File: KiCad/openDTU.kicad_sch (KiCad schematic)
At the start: 45 parts, among them J1 USB_C_Receptacle_USB2.0, J2 Conn_Coaxial, J3 Micro_SD_Card, Q1 BC817, Q2 BC817, SW1 SW_Push, SW2 SW_Push, U1 CH340C, U3 ESP32-WROOM-32, U4 nRF24L01P, U5 NCP1117-3.3_SOT223, Y1 Crystal

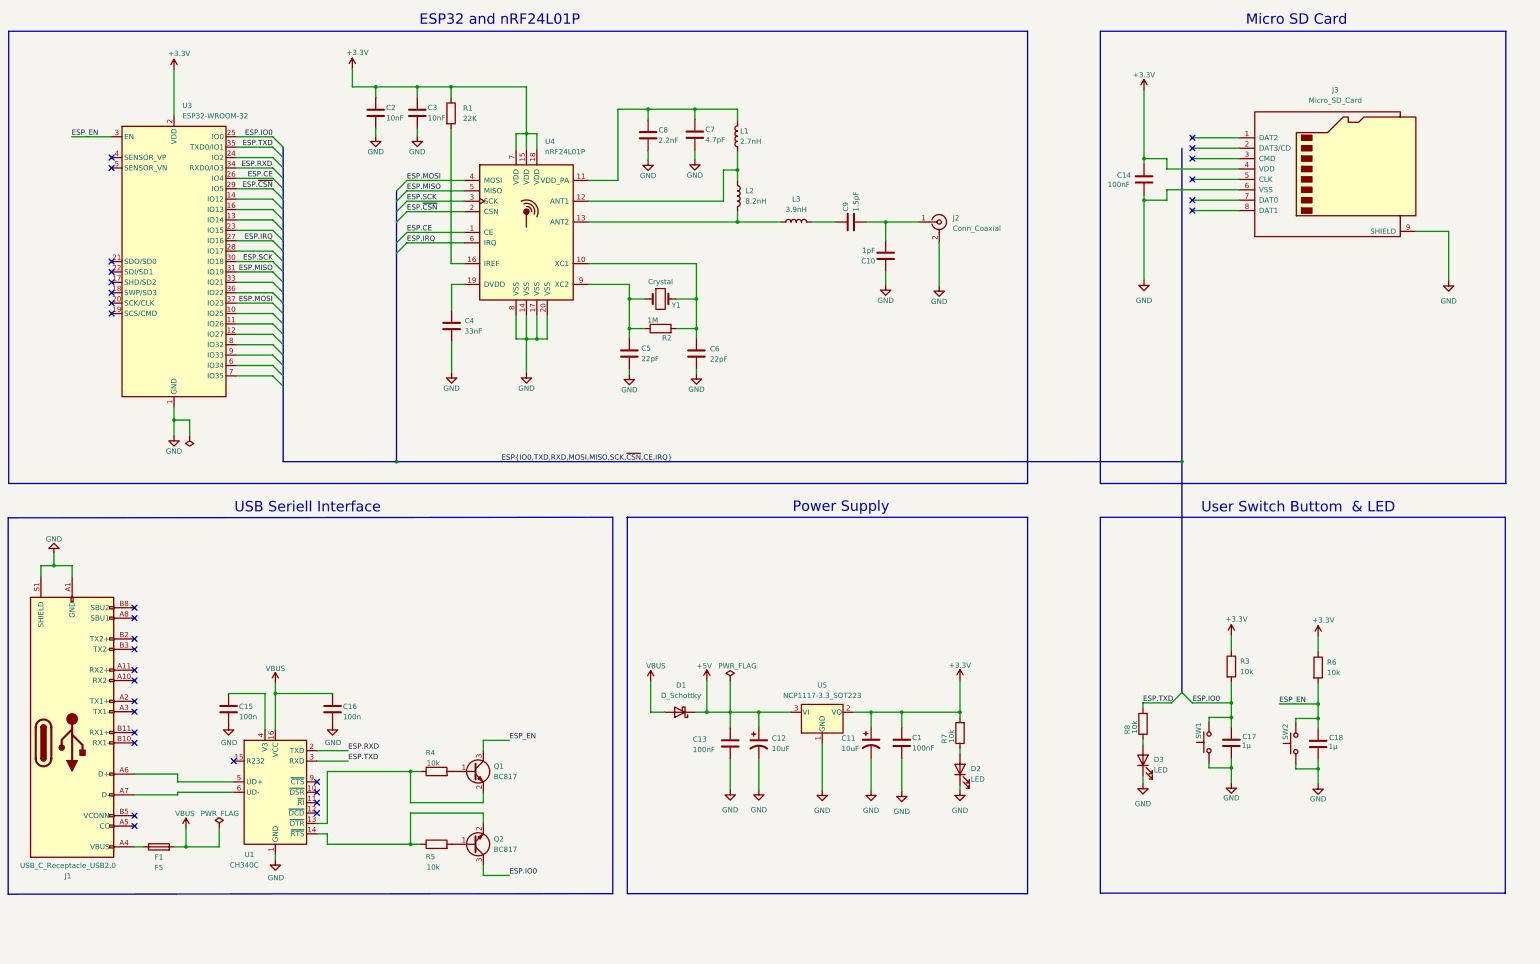
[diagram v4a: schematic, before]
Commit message: reduce the board size and beautify the placement
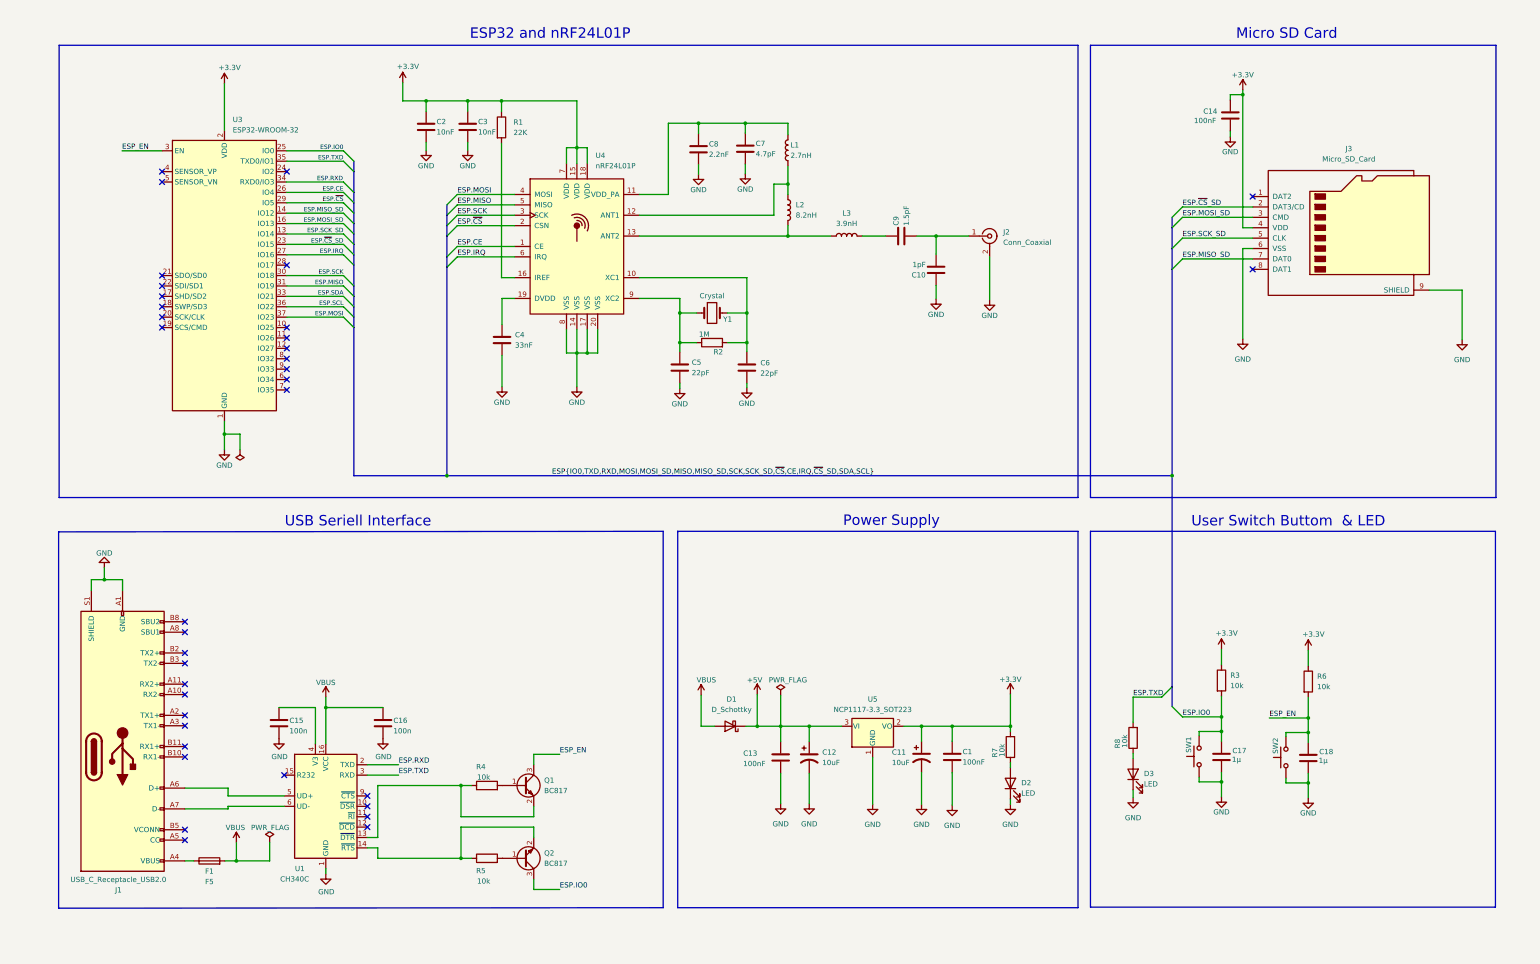
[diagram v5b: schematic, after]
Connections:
- net ESP.SCK_SD: now reaches U3.13 (IO14)
- net ESP.SCK_SD: now also J3.5 (CLK)
- net ESP.MISO_SD: now reaches U3.14 (IO12)
- net ESP.MISO_SD: now also J3.7 (DAT0)
- net ESP.MOSI_SD: now reaches U3.16 (IO13)
- net ESP.MOSI_SD: now also J3.3 (CMD)
- net ESP.~{CS}_SD: now reaches U3.23 (IO15)
- net ESP.~{CS}_SD: now also J3.2 (DAT3/CD)
- net ESP.SDA: now reaches U3.33 (IO21)
- net ESP.SCL: now reaches U3.36 (IO22)
- net ESP.~{CSN} renamed ESP.~{CS}
- no-connect marks 31 -> 36
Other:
- moved on the sheet: C1, C10, C11, C12, C13, C14, C15, C16, C17, C18, C2, C3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

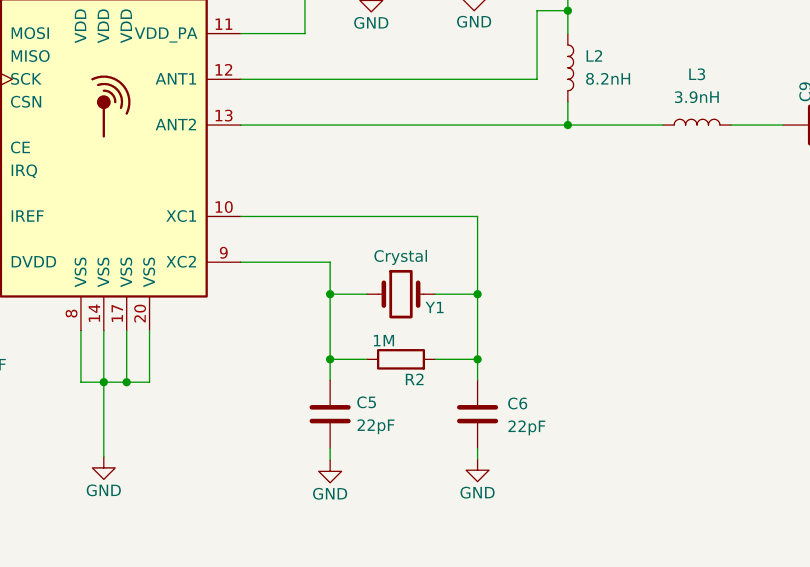
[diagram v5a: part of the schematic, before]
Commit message: routing first parts
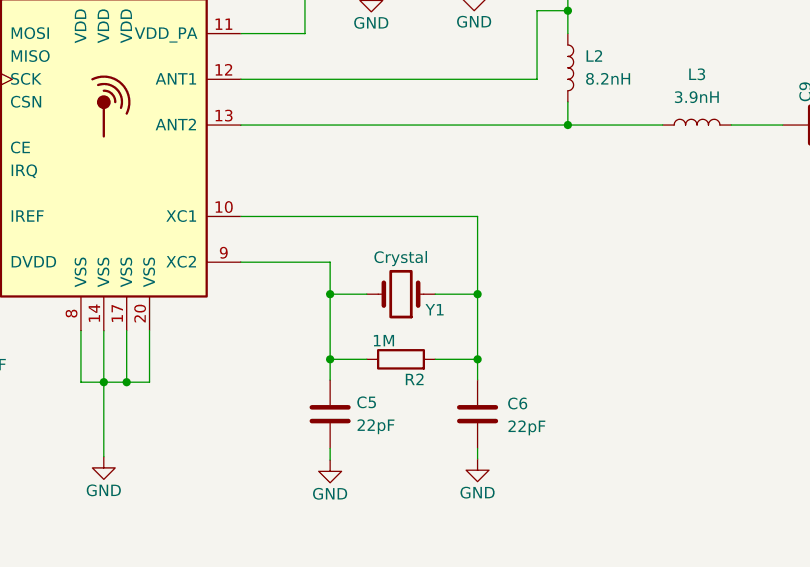
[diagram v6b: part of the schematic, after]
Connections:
- net at C5.1, R2.1, U4.9 (XC2): now also Y1.2; no longer Y1.1
- net at C6.1, R2.2, U4.10 (XC1): now also Y1.1; no longer Y1.2
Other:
- moved on the sheet: Y1
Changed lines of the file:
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@@
     (pin "1")
   )
-  (symbol (lib_id "Device:Crystal") (at 193.421 91.694 0) (unit 1)
+  (symbol (lib_id "Device:Crystal") (at 193.421 91.694 180) (unit 1)
     (in_bom yes) (on_board yes)
-    (property "Reference" "Y1" (id 0) (at 197.231 93.218 0))
-    (property "Value" "Crystal" (id 1) (at 193.421 87.503 0))
+    (property "Reference" "Y1" (id 0) (at 197.231 93.472 0))
+    (property "Value" "Crystal" (id 1) (at 193.421 87.63 0))
     (property "Footprint" "Crystal:Crystal_SMD_3225-4Pin_3.2x2.5mm" (id 2) (at 193.421 91.694 0)
       (effects (font (size 1.27 1.27)) hide)

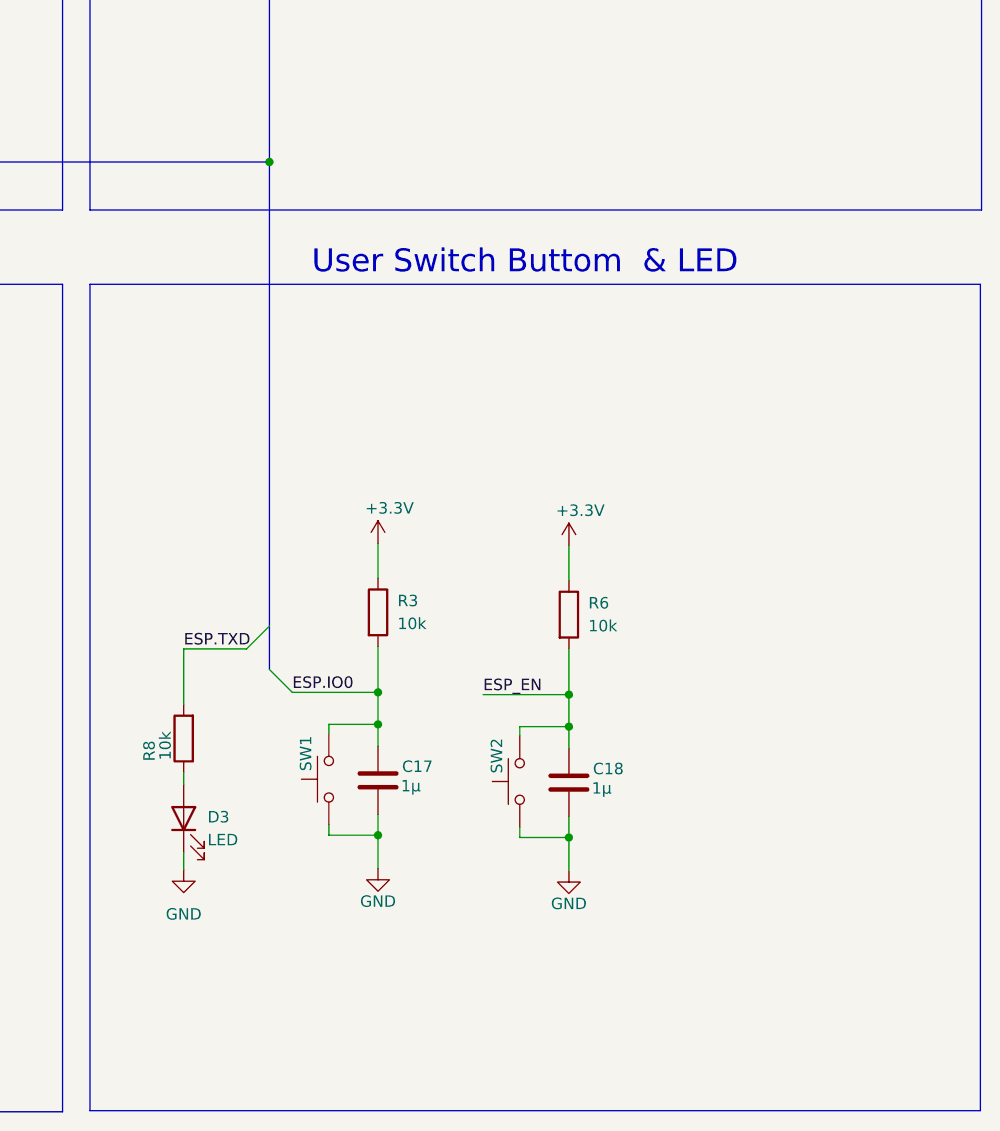
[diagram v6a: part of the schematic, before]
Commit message: adding pin header for I2C,SPI, etc.
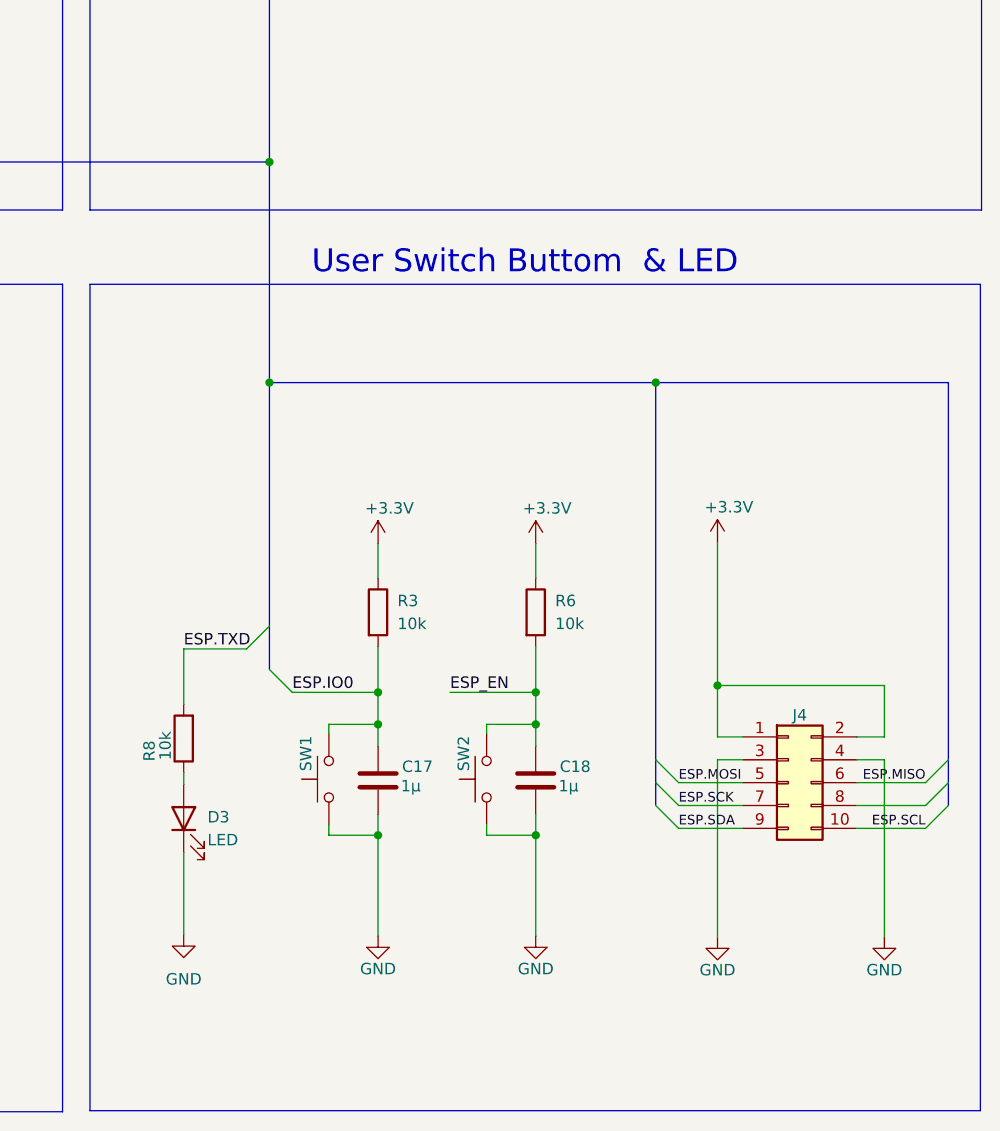
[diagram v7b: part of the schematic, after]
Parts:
- added J4: Conn_02x05_Counter_Clockwise, Connector_PinHeader_1.27mm:PinHeader_2x05_P1.27mm_Vertical, symbol Connector_Generic:Conn_02x05_Odd_Even
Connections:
- net +3.3V: now also J4.1 (Pin_1), J4.2 (Pin_2)
- net ESP.MISO: now also J4.6 (Pin_6)
- net ESP.MOSI: now also J4.5 (Pin_5)
- net ESP.SCK: now also J4.7 (Pin_7)
- net ESP.SCL: now also J4.10 (Pin_10)
- net ESP.SDA: now also J4.9 (Pin_9)
- net GND: now also J4.3 (Pin_3), J4.4 (Pin_4)
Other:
- moved on the sheet: C18, R6, SW2

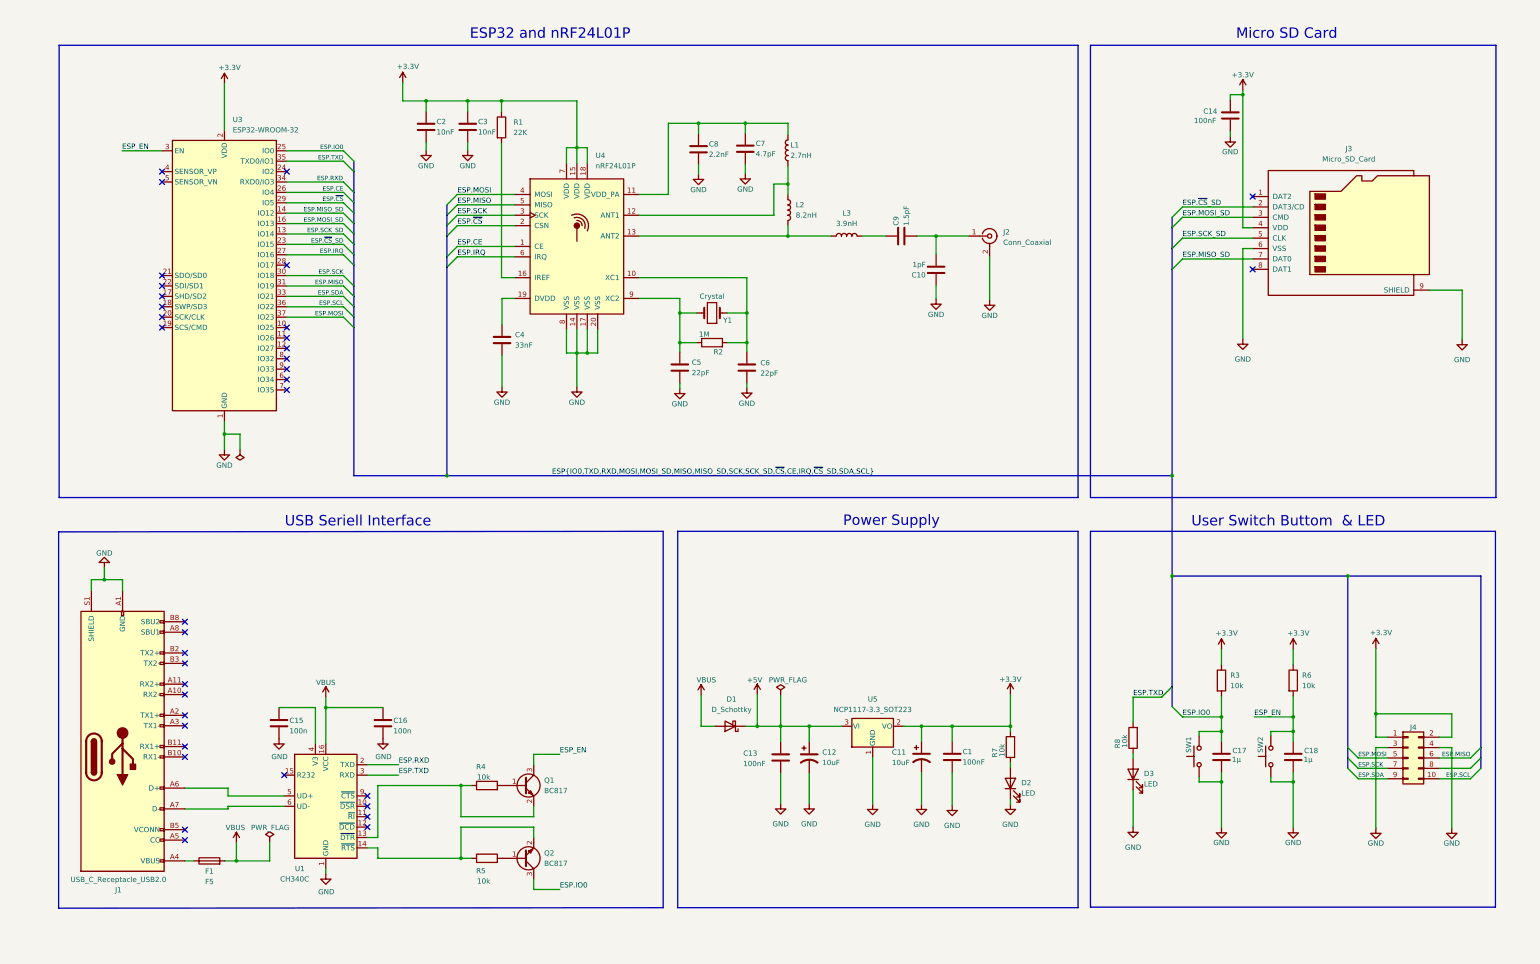
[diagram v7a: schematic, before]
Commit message: changing USB-C connector and switching GND and +3V3 inner layer
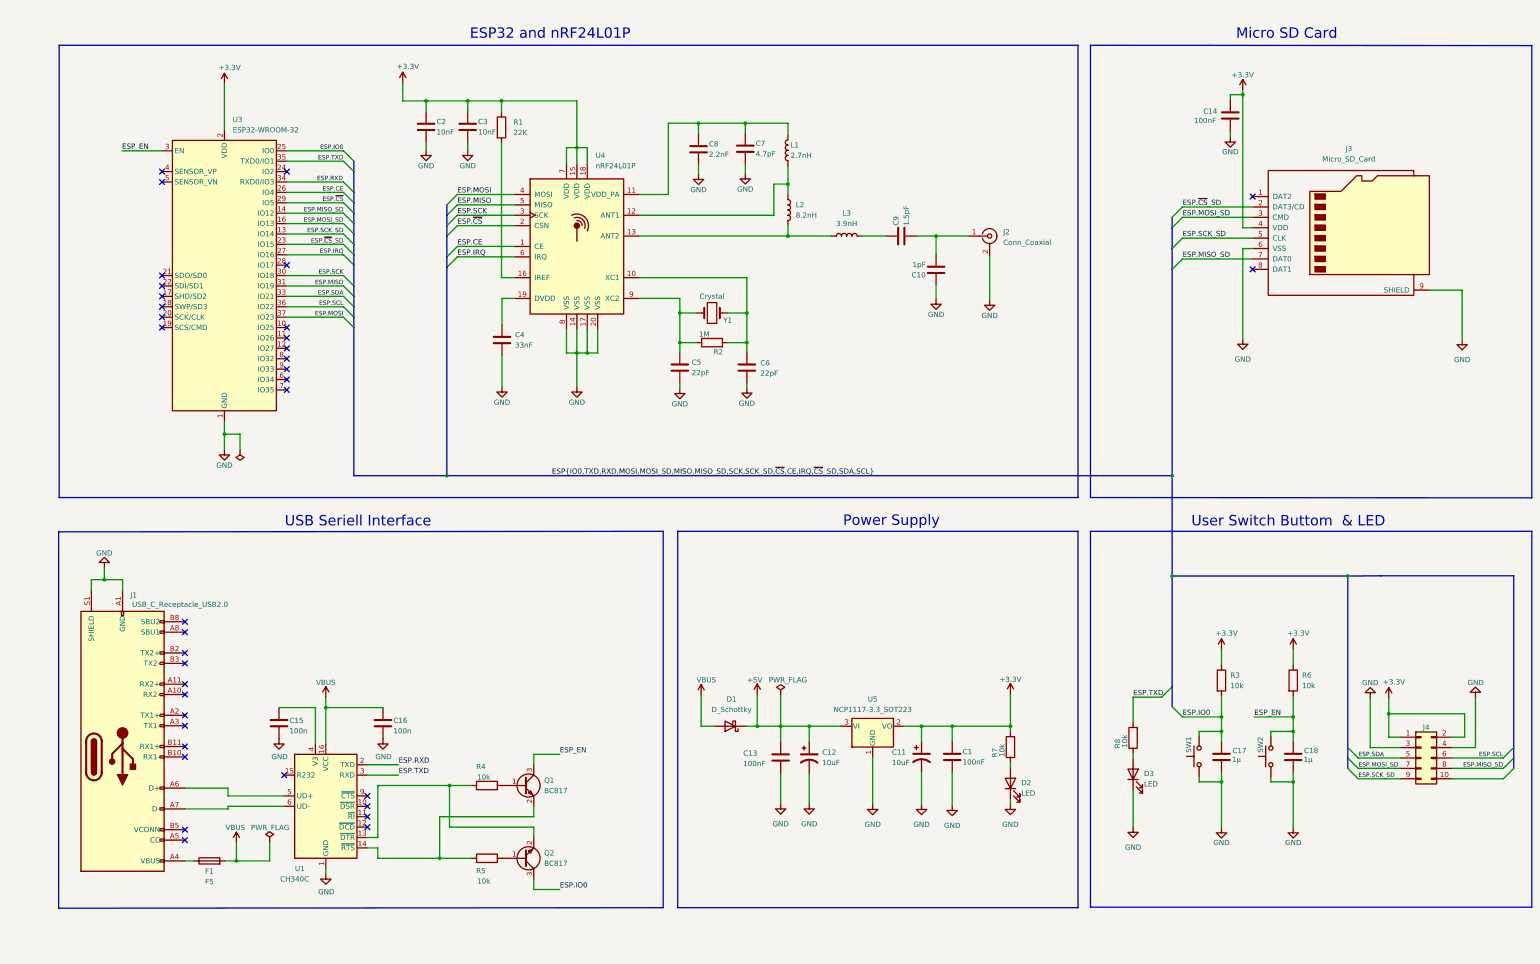
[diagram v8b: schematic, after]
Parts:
- J1: footprint Connector_USB:USB_C_Receptacle_GCT_USB4085 -> Connector_USB:USB_C_Receptacle_GCT_USB4105-xx-A_16P_TopMnt_Horizontal
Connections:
- net ESP.MISO: no longer J4.6 (Pin_6)
- net ESP.MISO_SD: now also J4.8 (Pin_8)
- net ESP.MOSI: no longer J4.5 (Pin_5)
- net ESP.MOSI_SD: now also J4.7 (Pin_7)
- net ESP.SCK: no longer J4.7 (Pin_7)
- net ESP.SCK_SD: now also J4.9 (Pin_9)
- net ESP.SCL: now also J4.6 (Pin_6); no longer J4.10 (Pin_10)
- net ESP.SDA: now also J4.5 (Pin_5); no longer J4.9 (Pin_9)
- net at R5.1, U1.14 (~{RTS}): now also Q1.2 (E); no longer Q2.2 (E)
- net at R4.1, U1.13 (~{DTR}): now also Q2.2 (E); no longer Q1.2 (E)
- net at J1.A6 (D+), U1.5 (UD+): now also J1.B6 (D+)
- net at J1.A7 (D-), U1.6 (UD-): now also J1.B7 (D-)
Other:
- moved on the sheet: J4
